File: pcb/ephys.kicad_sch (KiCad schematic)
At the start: 11 parts, among them U1 RHD2164, U13 NCP163AFCT330T2G

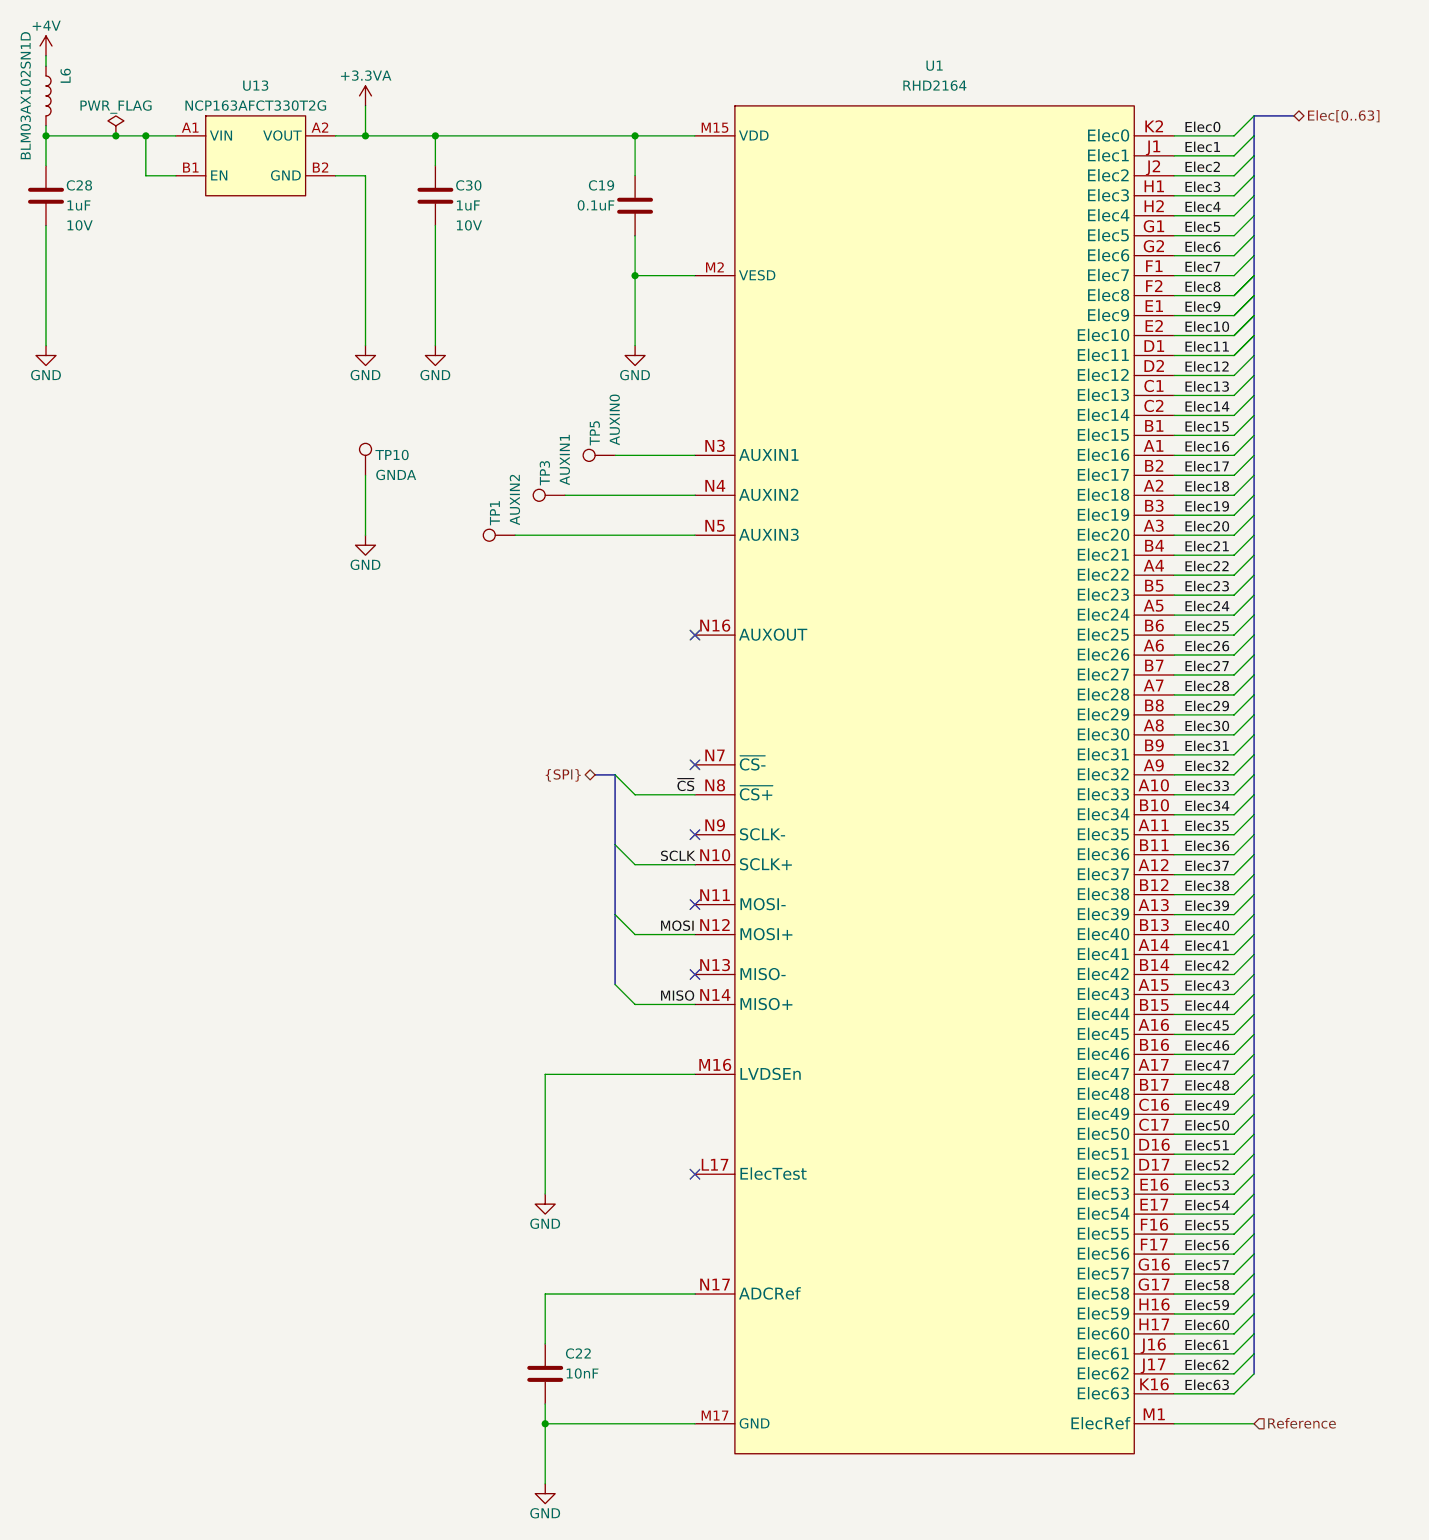
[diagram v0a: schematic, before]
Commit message: Rev. A initial design prior to fab comments
- BOM simplification
- Added my initials to the board
- Made the board more easy to panlize
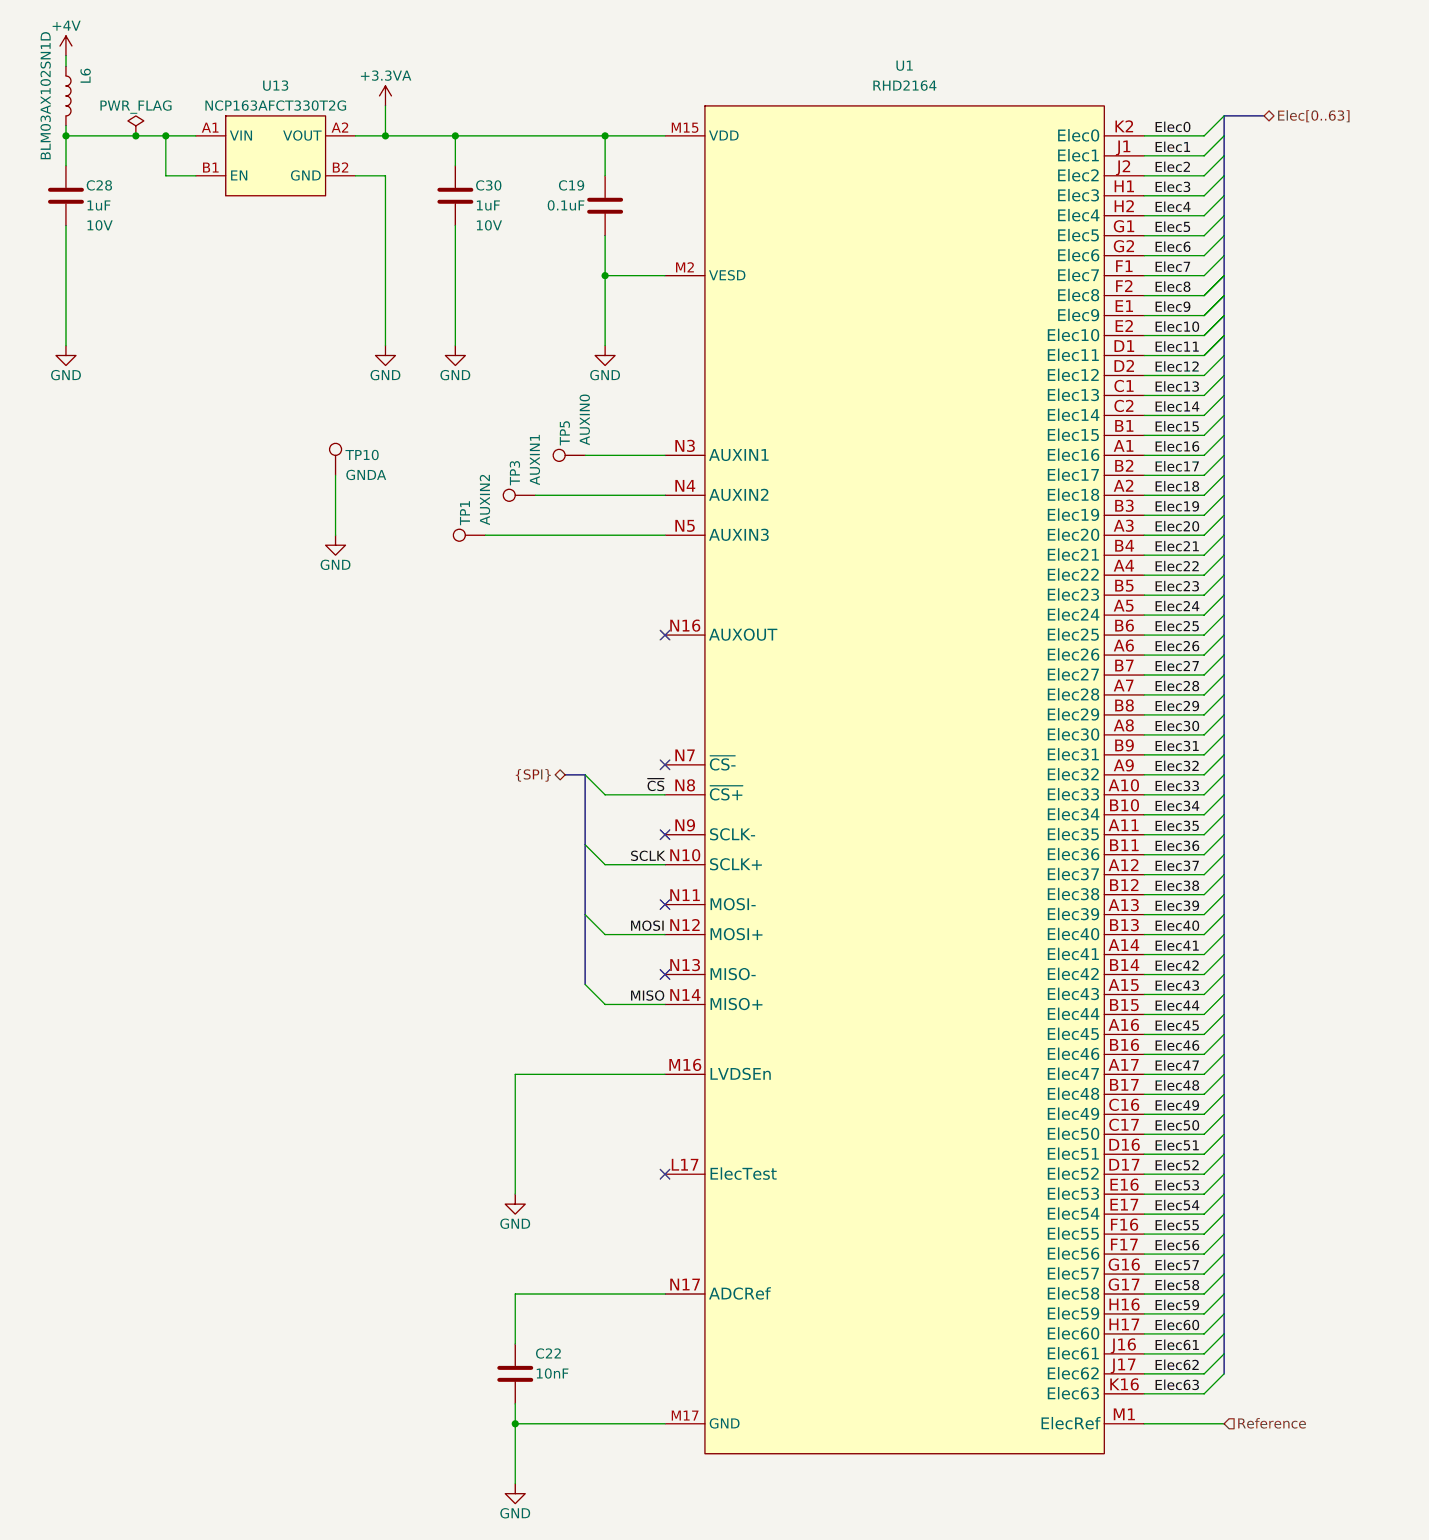
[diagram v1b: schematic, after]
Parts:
- TP1, TP10, TP3, TP5: now left out of the parts list
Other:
- moved on the sheet: C19, C22, C28, C30, L6, TP1, TP10, TP3, TP5, U1, U13

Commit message: Start of revision B
- Address the following issues
1. The photodiode anode is on pin 3, not pin 2
2. No paste on coax connector
3. CRESET_B needs to come out to programming header
4. Need PU on CS line.
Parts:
- C19: TempCo (none) -> X7R; Voltage (none) -> 16V
- C22: TempCo (none) -> X7R; Voltage (none) -> 35V
- C28, C30: TempCo (none) -> X5R
- TP1, TP10, TP3, TP5: DNP (none) -> DNP
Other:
- title: Headstage-RHS2116 -> Headstage-64s
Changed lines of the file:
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@@
   (paper "A4" portrait)
   (title_block
-    (title "Headstage-RHS2116")
+    (title "Headstage-64s")
     (date "2021-12-16")
-    (rev "A")
+    (rev "B")
     (company "Open Ephys, Inc")
     (comment 1 "Jonathan P. Newman")
@@
       (effects (font (size 1.27 1.27)) hide)
     )
+    (property "TempCo" "X7R" (id 4) (at 93.98 59.69 0)
+      (effects (font (size 1.27 1.27)) hide)
+    )
+    (property "Voltage" "16V" (id 5) (at 93.98 59.69 0)
+      (effects (font (size 1.27 1.27)) hide)
+    )
     (pin "1")
     (pin "2")
@@
     )
     (property "Datasheet" "~" (id 3) (at 91.44 86.36 0)
+      (effects (font (size 1.27 1.27)) hide)
+    )
+    (property "DNP" "DNP" (id 4) (at 91.44 91.44 0)
       (effects (font (size 1.27 1.27)) hide)
     )
@@
       (effects (font (size 1.27 1.27)) hide)
     )
-    (property "Datasheet" "" (id 3) (at 52.07 53.34 0)
+    (property "Datasheet" "~" (id 3) (at 52.07 53.34 0)
       (effects (font (size 1.27 1.27)) hide)
     )
@@
     (property "Voltage" "10V" (id 4) (at 27.94 62.23 0)
       (effects (font (size 1.27 1.27)) (justify left))
+    )
+    (property "TempCo" "X5R" (id 5) (at 25.4 58.42 0)
+      (effects (font (size 1.27 1.27)) hide)
     )
     (pin "1")
@@
       (effects (font (size 1.27 1.27)) hide)
     )
-    (property "Datasheet" "" (id 3) (at 119.38 39.37 0)
+    (property "Datasheet" "~" (id 3) (at 119.38 39.37 0)
       (effects (font (size 1.27 1.27)) hide)
     )
@@
       (effects (font (size 1.27 1.27)) hide)
     )
+    (property "DNP" "DNP" (id 4) (at 78.74 101.6 0)
+      (effects (font (size 1.27 1.27)) hide)
+    )
     (pin "1")
   )
@@
     )
     (property "Datasheet" "~" (id 3) (at 82.55 208.28 0)
+      (effects (font (size 1.27 1.27)) hide)
+    )
+    (property "TempCo" "X7R" (id 4) (at 82.55 208.28 0)
+      (effects (font (size 1.27 1.27)) hide)
+    )
+    (property "Voltage" "35V" (id 5) (at 82.55 208.28 0)
       (effects (font (size 1.27 1.27)) hide)
     )
@@
       (effects (font (size 1.27 1.27)) hide)
     )
+    (property "DNP" "DNP" (id 4) (at 59.69 93.98 0)
+      (effects (font (size 1.27 1.27)) hide)
+    )
     (pin "1")
   )
@@
       (effects (font (size 1.27 1.27)) hide)
     )
+    (property "DNP" "DNP" (id 4) (at 85.09 96.52 0)
+      (effects (font (size 1.27 1.27)) hide)
+    )
     (pin "1")
   )
@@
       (effects (font (size 1.27 1.27)) (justify left))
     )
-    (pin "1")
+    (property "TempCo" "X5R" (id 5) (at 74.93 58.42 0)
+      (effects (font (size 1.27 1.27)) hide)
+    )
+    (pin "1")
